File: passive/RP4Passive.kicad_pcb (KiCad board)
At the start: 2 copper layers, 30.4 x 56.8 mm, 8 parts, among them M1 Noctua

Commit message: update readme to version 6
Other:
- board text added: "RPiToHUB75 Adapter V6"
- board text removed: "RPiToHUB75 Adapter V5"
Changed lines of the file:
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@@
   (gr_line (start 166.13955 114.8543) (end 135.89 114.8543)
     (stroke (width 0.1) (type default)) (layer "Edge.Cuts"))
-  (gr_text "RPiToHUB75 Adapter V5\n" (at 138.938 112.268 90) (layer "F.SilkS")
+  (gr_text "RPiToHUB75 Adapter V6\n" (at 138.938 112.268 90) (layer "F.SilkS")
     (effects (font (size 1 1) (thickness 0.15)) (justify left bottom))
   )

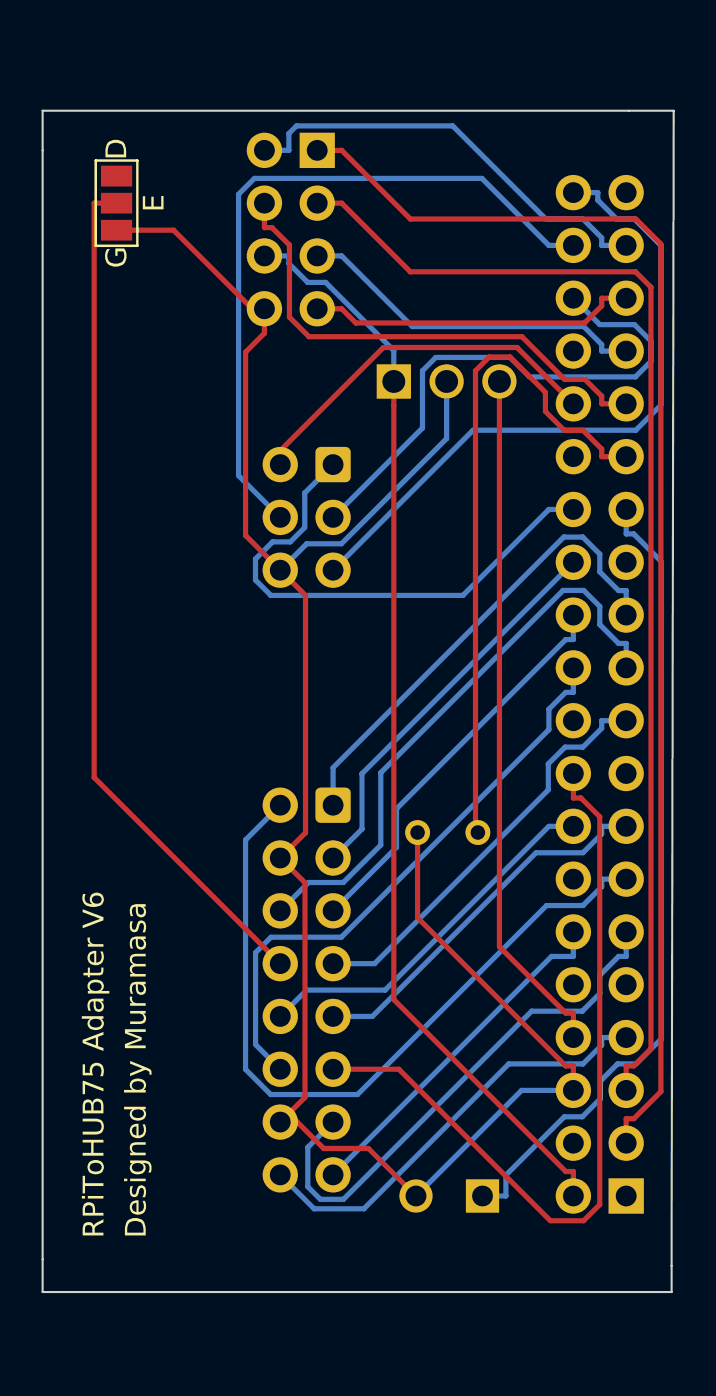
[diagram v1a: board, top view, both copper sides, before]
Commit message: add back 3.3v for the future co2 sensor
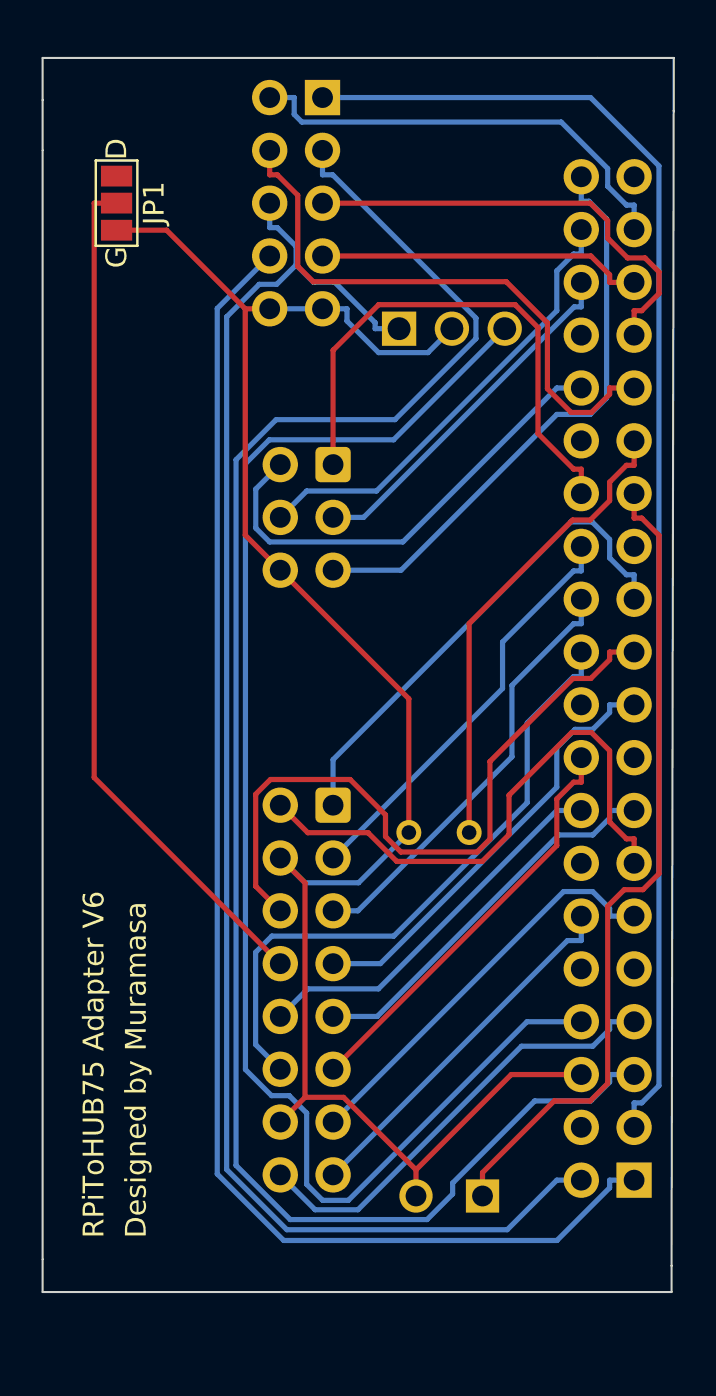
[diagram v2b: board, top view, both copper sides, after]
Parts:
- GPIO1: value 02x04 -> 02x05; footprint Connector_PinHeader_2.54mm:PinHeader_2x04_P2.54mm_Horizontal -> Connector_PinHeader_2.54mm:PinHeader_2x05_P2.54mm_Horizontal
- moved M1 2.55 mm to (153.0, 68.5)
- moved GPIO1 2.55 mm to (149.4, 57.4)
- moved RPiGPIO1 0.85 mm to (164.3, 109.5)
- moved S1 0.42 mm to (156.4, 92.8)
- renumbered E to JP1
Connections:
- net VCC renamed 5v
- GPIO1 pad 8: Net-(BZ1-+) -> 3.3v
- RPiGPIO1 pad 1: unconnected-(RPiGPIO1-Pin_1-Pad1) -> 3.3v
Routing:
- net 3.3v: track 0.00 -> 68.0 mm
- net FAN: track 33.2 -> 68.6 mm
- net GPIO 3: track 57.1 -> 83.9 mm
- net 5v: track 52.8 -> 74.7 mm
- net C: track 37.6 -> 20.1 mm
- net IO4: track 34.1 -> 22.0 mm
- net Net-(BZ1-+): track 97.6 -> 87.1 mm
- net TILT: track 32.5 -> 22.8 mm
- net G1: track 36.7 -> 27.1 mm
- net IO3: track 26.3 -> 17.3 mm
- net Clock: track 25.7 -> 19.8 mm
- net G2: track 27.8 -> 33.0 mm
- net GPIO 13: track 16.9 -> 21.8 mm
- net IO2: track 17.9 -> 22.5 mm
- net IO5: track 32.2 -> 27.9 mm
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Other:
- board size 30.4 x 56.8 mm -> 30.4 x 59.4 mm

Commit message: version 7
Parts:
- added J1: Conn_01x01, Custom:raspberrypi_2_3, B.Cu at (113.9, 81.5)
- added J2: Conn_01x02_Socket, Custom:JST_PH_S2B-PH-K_1x02_P2.00mm_Horizontal, B.Cu at (151.5, 59.1)
- added SCD30: Conn_01x04_Socket, Custom:STEMMA QT 1x04, B.Cu at (156.5, 57.8)
- GPIO1: value 02x05 -> 02x03; footprint Connector_PinHeader_2.54mm:PinHeader_2x05_P2.54mm_Horizontal -> Custom:GPIO Header
- HUB1: footprint Connector_IDC:IDC-Header_2x08_P2.54mm_Horizontal -> Custom:HUB75
- IO1: footprint Connector_IDC:IDC-Header_2x03_P2.54mm_Horizontal -> Custom:JST_SH_SM06B-SRSS-TB_1x06-1MP_P1.00mm_Horizontal
- RPiGPIO1: footprint Connector_PinSocket_2.54mm:PinSocket_2x20_P2.54mm_Vertical -> Custom:RPi GPIO
- moved IO1 39.5 mm to (162.7, 112.4), turned to -90 degrees
- moved BZ1 35.3 mm to (149.0, 75.9), turned to -90 degrees
- moved JP1 31.8 mm to (148.8, 92.8)
- moved GPIO1 27.7 mm to (149.2, 85.1)
- moved S1 21.6 mm to (147.1, 73.2), turned to 90 degrees
- moved HUB1 9.14 mm to (158.5, 94.5)
- moved M1 4.91 mm to (157.9, 67.8), turned to -90 degrees
- moved RPiGPIO1 3.81 mm to (164.2, 105.7)
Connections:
- GPIO1 pad 1: GPIO 2 -> GPIO 13
- GPIO1 pad 2: GPIO 26 -> GPIO 6
- GPIO1 pad 3: GPIO 3 -> GPIO 19
- GPIO1 pad 4: GPIO 6 -> 5v
- GPIO1 pad 5: GPIO 13 -> GPIO 26
- GPIO1 pad 6: 5v -> Net-(BZ1-+)
- RPiGPIO1 pad 1: 3.3v -> unconnected-(RPiGPIO1-Pin_1-Pad1)
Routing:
- net 3.3v: track 68.0 -> 0.00 mm
- net IO3: track 17.3 -> 71.6 mm, vias 0 -> 1
- net IO4: track 22.0 -> 71.6 mm, vias 0 -> 1
- net IO2: track 22.5 -> 69.1 mm, vias 0 -> 1
- net IO5: track 27.9 -> 70.1 mm, vias 0 -> 1
- net 5v: track 74.7 -> 105.6 mm
- net GPIO 19: track 15.7 -> 44.7 mm, vias 0 -> 1
- net FAN: track 68.6 -> 39.9 mm, vias 0 -> 3
- net GPIO 3: track 83.9 -> 56.7 mm, vias 0 -> 1
- net Net-(HUB1-Pin_8): track 41.4 -> 14.2 mm
- net BUZZ: track 39.6 -> 16.9 mm
- net IO1: track 25.8 -> 45.3 mm
- net GPIO 2: track 64.5 -> 83.6 mm, vias 0 -> 1
- net GPIO 26: track 21.8 -> 39.8 mm, vias 0 -> 1
- net G1: track 27.1 -> 13.4 mm
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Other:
- board size 30.4 x 59.4 mm -> 20.9 x 63 mm
- board text added: "26 19 13 G- 5v 6"
- board text added: "RPiToHUB75 Adapter V7"
- board text removed: "RPiToHUB75 Adapter V6"

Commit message: update image
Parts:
- J2: value Conn_01x02_Socket -> 1x02
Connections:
- J2 pad 1: unconnected-(J2-Pin_1-Pad1) -> 5v
- J2 pad 2: unconnected-(J2-Pin_2-Pad2) -> Net-(BZ1-+)
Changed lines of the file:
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@@
   (net 41 "5v")
   (net 42 "unconnected-(RPiGPIO1-Pin_1-Pad1)")
-  (net 43 "unconnected-(J2-Pin_1-Pad1)")
-  (net 44 "unconnected-(J2-Pin_2-Pad2)")
   (footprint "Jumper:SolderJumper-3_P1.3mm_Open_Pad1.0x1.5mm_NumberLabels" (layer "F.Cu")
     (at 148.844 92.837 -90)
@@
       (stroke (width 0.05) (type default)) (fill none) (layer "B.CrtYd"))
     (model "C:/Users/Admin/Downloads/RASPBERRY_PI_5.STEP/RASPBERRY_PI_5.STEP"
-      (offset (xyz 10 -24.5 12.5))
+      (opacity 0.0000)      (offset (xyz 10 -24.5 12.5))
       (scale (xyz 1 1 1))
       (rotate (xyz 90 0 0))
     )
     (model "C:/Users/Admin/Downloads/black-aluminum-heatsink-for-raspberry-pi-1.snapshot.3/Heat sink Al.step"
-      (offset (xyz 0.5 -19 7.5))
+      (opacity 0.0000)      (offset (xyz 0.5 -19 7.5))
       (scale (xyz 1 1 1))
       (rotate (xyz 90 0 0))
@@
         (effects (font (size 1 1) (thickness 0.15)) (justify mirror))
     )
-    (fp_text value "Conn_01x02_Socket" (at 1 -7.45 90) (layer "B.Fab") hide
+    (fp_text value "1x02" (at 1 -7.45 90) (layer "B.Fab") hide
         (effects (font (size 1 1) (thickness 0.15)) (justify mirror))
     )
@@
       (stroke (width 0.1) (type solid)) (layer "B.Fab"))
     (pad "1" thru_hole roundrect (at 0 0 90) (size 1.2 1.75) (drill 0.75) (layers "*.Cu" "*.Mask") (roundrect_rratio 0.208333)
-      (net 43 "unconnected-(J2-Pin_1-Pad1)") (pinfunction "Pin_1") (pintype "passive+no_connect"))
+      (net 41 "5v") (pinfunction "Pin_1") (pintype "passive"))
     (pad "2" thru_hole oval (at 2 0 90) (size 1.2 1.75) (drill 0.75) (layers "*.Cu" "*.Mask")
-      (net 44 "unconnected-(J2-Pin_2-Pad2)") (pinfunction "Pin_2") (pintype "passive+no_connect"))
+      (net 2 "Net-(BZ1-+)") (pinfunction "Pin_2") (pintype "passive"))
     (model "${KICAD6_3DMODEL_DIR}/Connector_JST.3dshapes/JST_PH_S2B-PH-K_1x02_P2.00mm_Horizontal.wrl"
       (offset (xyz 0 0 0))
